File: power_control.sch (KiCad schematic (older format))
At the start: 80 parts, among them J1 Conn_01x02, J2 Conn_01x02, J28 Conn_01x02, J29 Conn_01x02, J30 Conn_01x02, J4 Conn_01x02, J5 Conn_01x02, J6 Conn_01x02, U1 L6203, U10 L6203, U11 L6203, U12 L6203, U3 L6203, U5 L6203, U6 L6203, U7 L6203

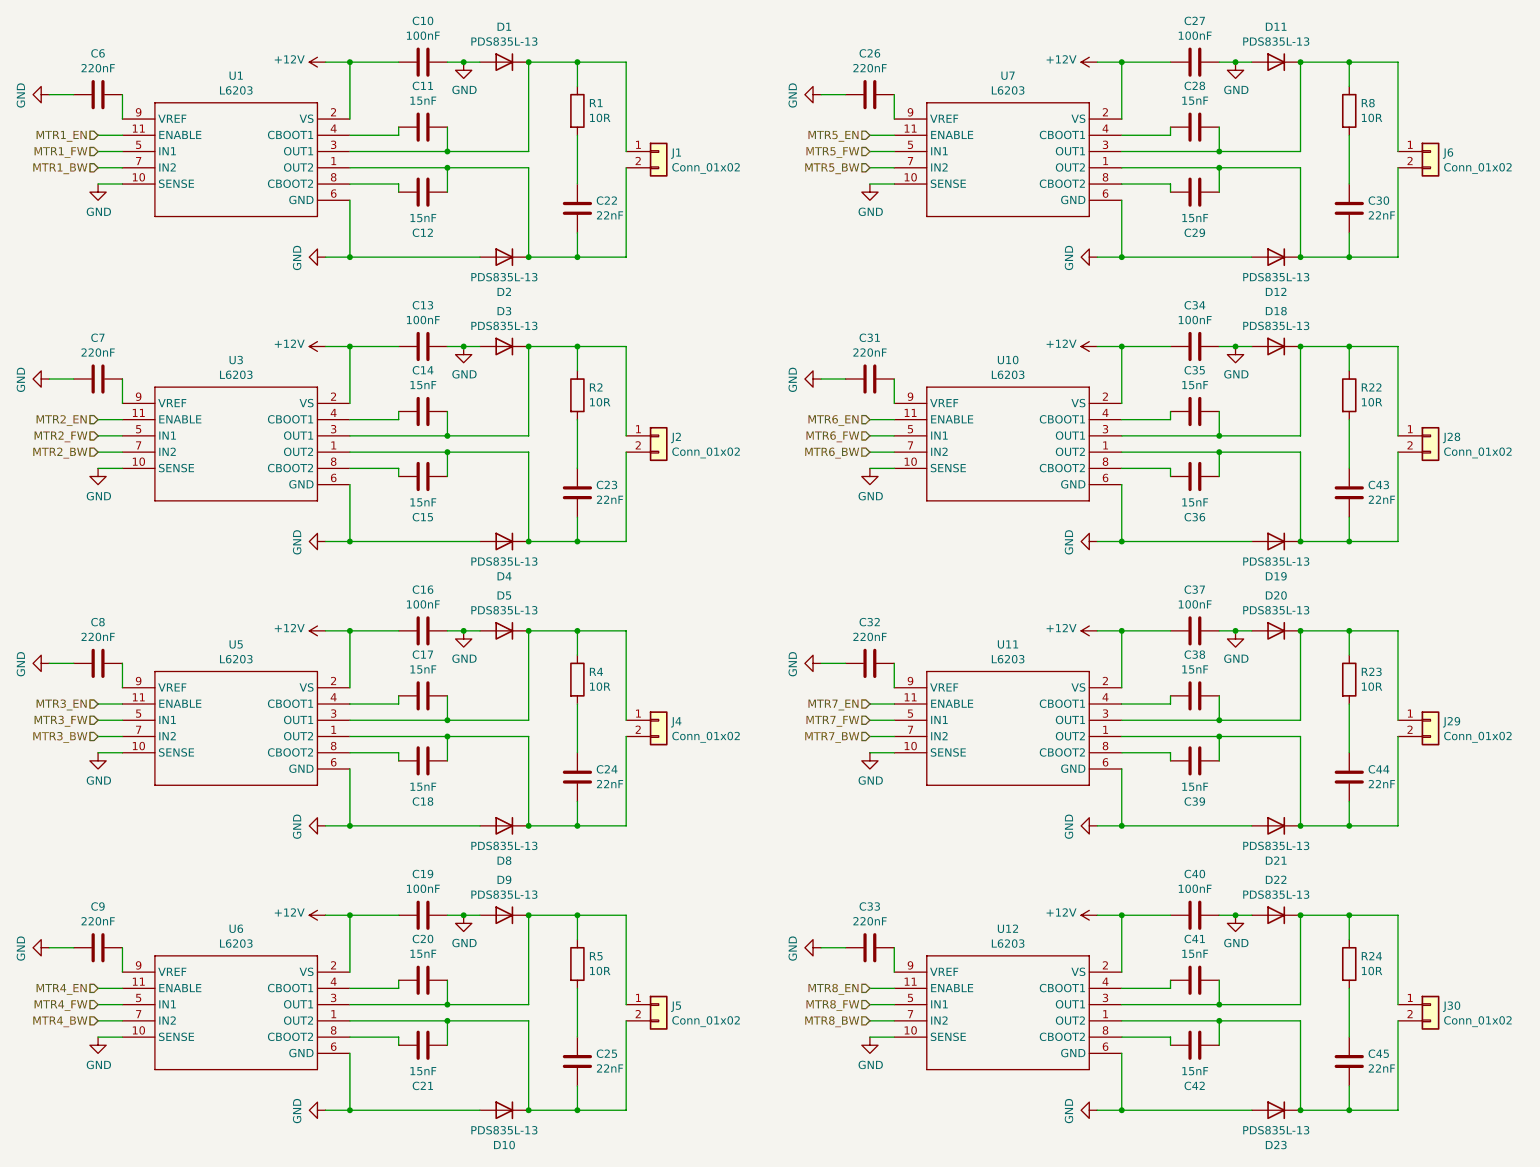
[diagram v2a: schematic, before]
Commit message: Positioning finished
Lacks fine alignment.
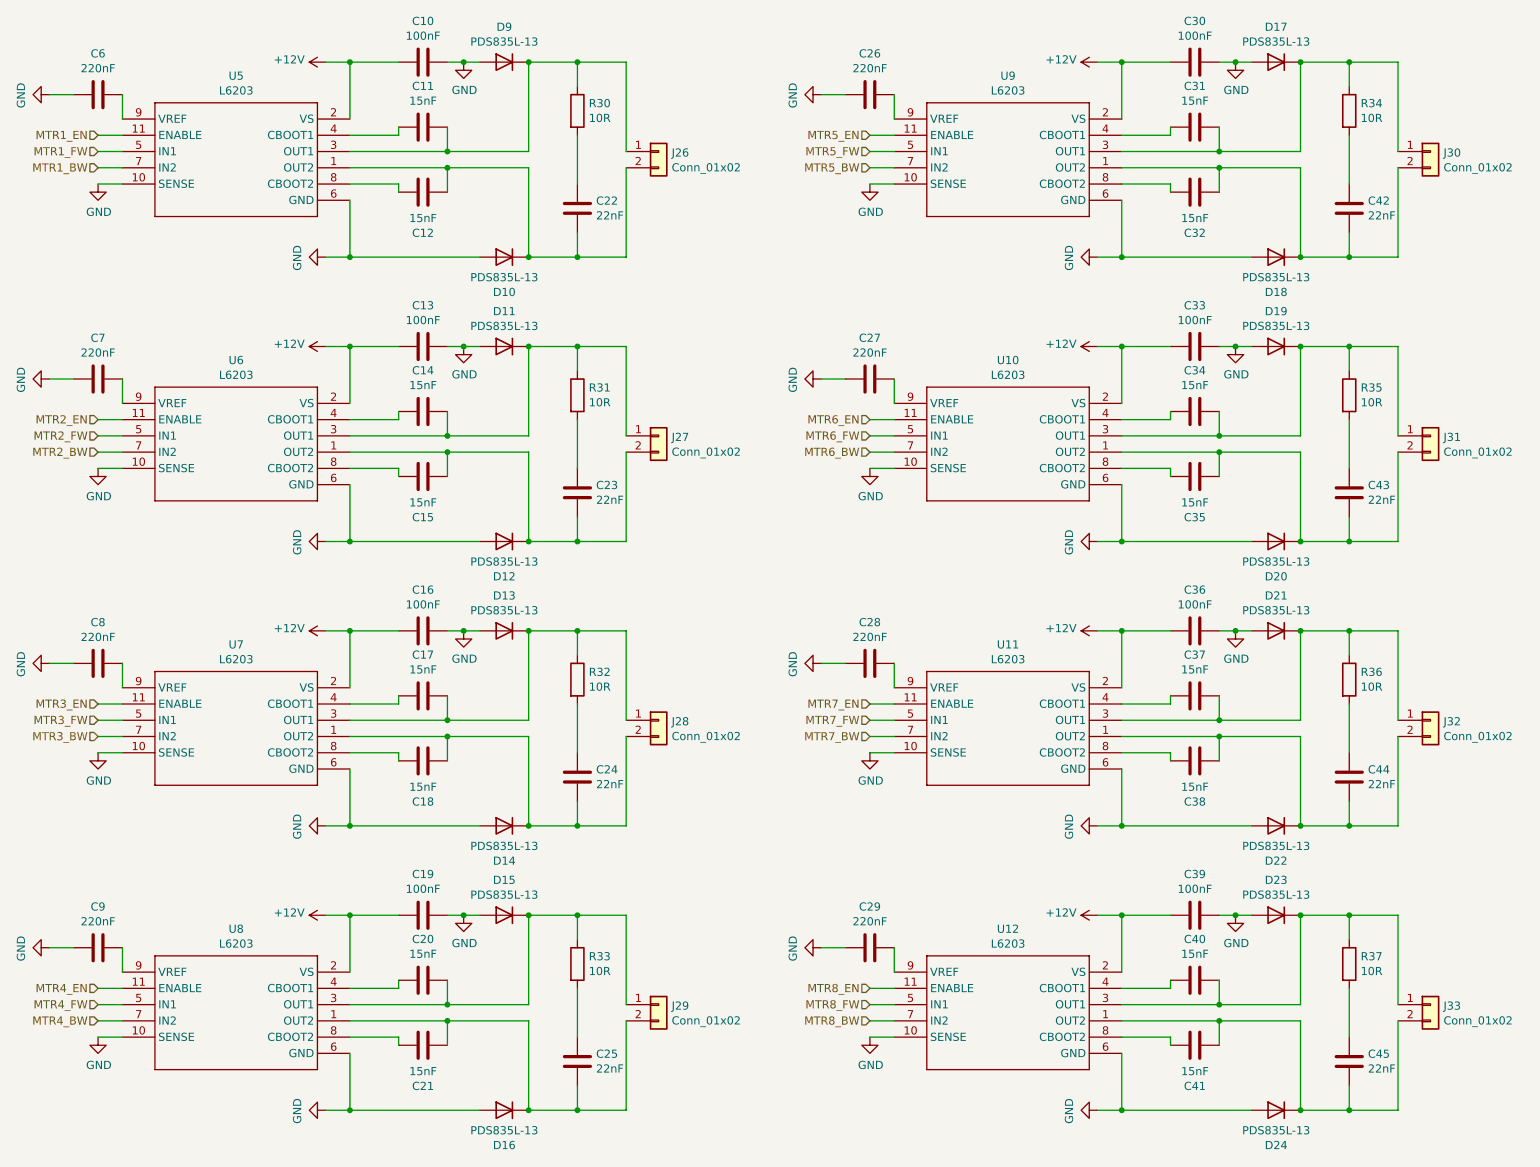
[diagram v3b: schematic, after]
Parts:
- renumbered C31 to C27, C32 to C28, C33 to C29, C27 to C30, C28 to C31, C29 to C32, C34 to C33, C35 to C34, C36 to C35, C37 to C36, C38 to C37, C39 to C38, C40 to C39, C41 to C40, C42 to C41, C30 to C42, D2 to D10, D3 to D11, D4 to D12, D5 to D13, D8 to D14, D9 to D15, D10 to D16, D11 to D17, D12 to D18, D18 to D19, D19 to D20, D20 to D21, D21 to D22, D22 to D23, D23 to D24, D1 to D9, J1 to J26, J2 to J27, J4 to J28, J5 to J29, J6 to J30, J28 to J31, J29 to J32, J30 to J33, R1 to R30, R2 to R31, R4 to R32, R5 to R33, R8 to R34, R22 to R35, R23 to R36, R24 to R37, U1 to U5, U3 to U6, U5 to U7, U6 to U8, U7 to U9

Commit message: Start MCU layout
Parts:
- renumbered C6 to C11, C7 to C12, C8 to C13, C9 to C14, C10 to C15, C11 to C16, C12 to C17, C13 to C18, C14 to C19, C15 to C20, C16 to C21, C17 to C22, C18 to C23, C19 to C24, C20 to C25, C21 to C26, C22 to C27, C23 to C28, C24 to C29, C25 to C30, C26 to C31, C27 to C32, C28 to C33, C29 to C34, C30 to C35, C31 to C36, C32 to C37, C33 to C38, C34 to C39, C35 to C40, C36 to C41, C37 to C42, C38 to C43, C39 to C44, C40 to C45, C41 to C46, C42 to C47, C43 to C48, C44 to C49, C45 to C50, J26 to J27, J27 to J28, J28 to J29, J29 to J30, J30 to J31, J31 to J32, J32 to J33, J33 to J34

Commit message: Stash
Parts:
- renumbered J27 to J26, J28 to J27, J29 to J28, J30 to J29, J31 to J30, J32 to J31, J33 to J32, J34 to J33
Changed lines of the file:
@@
 P 4450 6550
 AR Path="/5E1FFE0F" Ref="J?"  Part="1"
-AR Path="/5E1C04CF/5E1FFE0F" Ref="J30"  Part="1"
+AR Path="/5E1C04CF/5E1FFE0F" Ref="J29"  Part="1"
 AR Path="/5E3E0C4B/5E1FFE0F" Ref="J?"  Part="1"
-F 0 "J30" H 4530 6542 50  0000 L CNN
+F 0 "J29" H 4530 6542 50  0000 L CNN
 F 1 "Conn_01x02" H 4530 6451 50  0000 L CNN
 F 2 "Connector_Molex:Molex_Micro-Fit_3.0_43045-0212_2x01_P3.00mm_Vertical" H 4450 6550 50  0001 C CNN
@@
 P 4450 4800
 AR Path="/5E4C5662" Ref="J?"  Part="1"
-AR Path="/5E1C04CF/5E4C5662" Ref="J29"  Part="1"
+AR Path="/5E1C04CF/5E4C5662" Ref="J28"  Part="1"
 AR Path="/5E3E0C4B/5E4C5662" Ref="J?"  Part="1"
-F 0 "J29" H 4530 4792 50  0000 L CNN
+F 0 "J28" H 4530 4792 50  0000 L CNN
 F 1 "Conn_01x02" H 4530 4701 50  0000 L CNN
 F 2 "Connector_Molex:Molex_Micro-Fit_3.0_43045-0212_2x01_P3.00mm_Vertical" H 4450 4800 50  0001 C CNN
@@
 P 4450 3050
 AR Path="/5E4D6D0D" Ref="J?"  Part="1"
-AR Path="/5E1C04CF/5E4D6D0D" Ref="J28"  Part="1"
+AR Path="/5E1C04CF/5E4D6D0D" Ref="J27"  Part="1"
 AR Path="/5E3E0C4B/5E4D6D0D" Ref="J?"  Part="1"
-F 0 "J28" H 4530 3042 50  0000 L CNN
+F 0 "J27" H 4530 3042 50  0000 L CNN
 F 1 "Conn_01x02" H 4530 2951 50  0000 L CNN
 F 2 "Connector_Molex:Molex_Micro-Fit_3.0_43045-0212_2x01_P3.00mm_Vertical" H 4450 3050 50  0001 C CNN
@@
 P 9200 1300
 AR Path="/5E50C463" Ref="J?"  Part="1"
-AR Path="/5E1C04CF/5E50C463" Ref="J31"  Part="1"
+AR Path="/5E1C04CF/5E50C463" Ref="J30"  Part="1"
 AR Path="/5E3E0C4B/5E50C463" Ref="J?"  Part="1"
-F 0 "J31" H 9280 1292 50  0000 L CNN
+F 0 "J30" H 9280 1292 50  0000 L CNN
 F 1 "Conn_01x02" H 9280 1201 50  0000 L CNN
 F 2 "Connector_Molex:Molex_Micro-Fit_3.0_43045-0212_2x01_P3.00mm_Vertical" H 9200 1300 50  0001 C CNN
@@
 P 9200 6550
 AR Path="/5E42316A" Ref="J?"  Part="1"
-AR Path="/5E1C04CF/5E42316A" Ref="J34"  Part="1"
+AR Path="/5E1C04CF/5E42316A" Ref="J33"  Part="1"
 AR Path="/5E3E0C4B/5E42316A" Ref="J?"  Part="1"
-F 0 "J34" H 9280 6542 50  0000 L CNN
+F 0 "J33" H 9280 6542 50  0000 L CNN
 F 1 "Conn_01x02" H 9280 6451 50  0000 L CNN
 F 2 "Connector_Molex:Molex_Micro-Fit_3.0_43045-0212_2x01_P3.00mm_Vertical" H 9200 6550 50  0001 C CNN
@@
 P 9200 4800
 AR Path="/5E4231F1" Ref="J?"  Part="1"
-AR Path="/5E1C04CF/5E4231F1" Ref="J33"  Part="1"
+AR Path="/5E1C04CF/5E4231F1" Ref="J32"  Part="1"
 AR Path="/5E3E0C4B/5E4231F1" Ref="J?"  Part="1"
-F 0 "J33" H 9280 4792 50  0000 L CNN
+F 0 "J32" H 9280 4792 50  0000 L CNN
 F 1 "Conn_01x02" H 9280 4701 50  0000 L CNN
 F 2 "Connector_Molex:Molex_Micro-Fit_3.0_43045-0212_2x01_P3.00mm_Vertical" H 9200 4800 50  0001 C CNN
@@
 P 9200 3050
 AR Path="/5E42327E" Ref="J?"  Part="1"
-AR Path="/5E1C04CF/5E42327E" Ref="J32"  Part="1"
+AR Path="/5E1C04CF/5E42327E" Ref="J31"  Part="1"
 AR Path="/5E3E0C4B/5E42327E" Ref="J?"  Part="1"
-F 0 "J32" H 9280 3042 50  0000 L CNN
+F 0 "J31" H 9280 3042 50  0000 L CNN
 F 1 "Conn_01x02" H 9280 2951 50  0000 L CNN
 F 2 "Connector_Molex:Molex_Micro-Fit_3.0_43045-0212_2x01_P3.00mm_Vertical" H 9200 3050 50  0001 C CNN
@@
 P 4450 1300
 AR Path="/5E4D6D98" Ref="J?"  Part="1"
-AR Path="/5E1C04CF/5E4D6D98" Ref="J27"  Part="1"
+AR Path="/5E1C04CF/5E4D6D98" Ref="J26"  Part="1"
 AR Path="/5E3E0C4B/5E4D6D98" Ref="J?"  Part="1"
-F 0 "J27" H 4530 1292 50  0000 L CNN
+F 0 "J26" H 4530 1292 50  0000 L CNN
 F 1 "Conn_01x02" H 4530 1201 50  0000 L CNN
 F 2 "Connector_Molex:Molex_Micro-Fit_3.0_43045-0212_2x01_P3.00mm_Vertical" H 4450 1300 50  0001 C CNN

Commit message: Added capacitor references
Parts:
- C11, C12, C13, C14, C31, C32, C33, C34: manf# (none) -> EMK107B7224KA-T
- C15, C18, C21, C24, C35, C38, C41, C44: manf# (none) -> EMK107B7104KAHT
- C16, C17, C19, C20, C22, C23, C25, C26, C36, C37, C39, C40, C42, C43, C45, C46: manf# (none) -> C0603C153M4RECTU
- C27, C28, C29, C30, C47, C48, C49, C50: manf# (none) -> C0603C223K4RACTU
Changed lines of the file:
@@
 F 2 "lsts-passives:C_0603" H 1038 6050 50  0001 C CNN
 F 3 "~" H 1000 6200 50  0001 C CNN
+F 4 "EMK107B7224KA-T" H 1000 6200 50  0001 C CNN "manf#"
 	1    1000 6200
 	0    1    1    0
@@
 F 2 "lsts-passives:C_0603" H 3988 6750 50  0001 C CNN
 F 3 "~" H 3950 6900 50  0001 C CNN
+F 4 "C0603C223K4RACTU" H 3950 6900 50  0001 C CNN "manf#"
 	1    3950 6900
 	1    0    0    -1
@@
 F 2 "lsts-passives:C_0603" H 3038 6250 50  0001 C CNN
 F 3 "~" H 3000 6400 50  0001 C CNN
+F 4 "C0603C153M4RECTU" H 3000 6400 50  0001 C CNN "manf#"
 	1    3000 6400
 	0    1    1    0
@@
 F 2 "lsts-passives:C_0603" H 3038 6650 50  0001 C CNN
 F 3 "~" H 3000 6800 50  0001 C CNN
+F 4 "C0603C153M4RECTU" H 3000 6800 50  0001 C CNN "manf#"
 	1    3000 6800
 	0    1    -1   0
@@
 F 2 "lsts-passives:C_0603" H 3038 5850 50  0001 C CNN
 F 3 "~" H 3000 6000 50  0001 C CNN
+F 4 "EMK107B7104KAHT" H 3000 6000 50  0001 C CNN "manf#"
 	1    3000 6000
 	0    1    1    0
@@
 F 2 "lsts-passives:C_0603" H 1038 4300 50  0001 C CNN
 F 3 "~" H 1000 4450 50  0001 C CNN
+F 4 "EMK107B7224KA-T" H 1000 4450 50  0001 C CNN "manf#"
 	1    1000 4450
 	0    1    1    0
@@
 F 2 "lsts-passives:C_0603" H 3038 4500 50  0001 C CNN
 F 3 "~" H 3000 4650 50  0001 C CNN
+F 4 "C0603C153M4RECTU" H 3000 4650 50  0001 C CNN "manf#"
 	1    3000 4650
 	0    1    1    0
@@
 F 2 "lsts-passives:C_0603" H 3038 4900 50  0001 C CNN
 F 3 "~" H 3000 5050 50  0001 C CNN
+F 4 "C0603C153M4RECTU" H 3000 5050 50  0001 C CNN "manf#"
 	1    3000 5050
 	0    1    -1   0
@@
 F 2 "lsts-passives:C_0603" H 3038 4100 50  0001 C CNN
 F 3 "~" H 3000 4250 50  0001 C CNN
+F 4 "EMK107B7104KAHT" H 3000 4250 50  0001 C CNN "manf#"
 	1    3000 4250
 	0    1    1    0
@@
 F 2 "lsts-passives:C_0603" H 1038 2550 50  0001 C CNN
 F 3 "~" H 1000 2700 50  0001 C CNN
+F 4 "EMK107B7224KA-T" H 1000 2700 50  0001 C CNN "manf#"
 	1    1000 2700
 	0    1    1    0
@@
 F 2 "lsts-passives:C_0603" H 3988 3250 50  0001 C CNN
 F 3 "~" H 3950 3400 50  0001 C CNN
+F 4 "C0603C223K4RACTU" H 3950 3400 50  0001 C CNN "manf#"
 	1    3950 3400
 	1    0    0    -1
@@
 F 2 "lsts-passives:C_0603" H 3038 2750 50  0001 C CNN
 F 3 "~" H 3000 2900 50  0001 C CNN
+F 4 "C0603C153M4RECTU" H 3000 2900 50  0001 C CNN "manf#"
 	1    3000 2900
 	0    1    1    0
@@
 F 2 "lsts-passives:C_0603" H 3038 3150 50  0001 C CNN
 F 3 "~" H 3000 3300 50  0001 C CNN
+F 4 "C0603C153M4RECTU" H 3000 3300 50  0001 C CNN "manf#"
 	1    3000 3300
 	0    1    -1   0
@@
 F 2 "lsts-passives:C_0603" H 3038 2350 50  0001 C CNN
 F 3 "~" H 3000 2500 50  0001 C CNN
+F 4 "EMK107B7104KAHT" H 3000 2500 50  0001 C CNN "manf#"
 	1    3000 2500
 	0    1    1    0
@@
 F 2 "lsts-passives:C_0603" H 5788 800 50  0001 C CNN
 F 3 "~" H 5750 950 50  0001 C CNN
+F 4 "EMK107B7224KA-T" H 5750 950 50  0001 C CNN "manf#"
 	1    5750 950
 	0    1    1    0
@@
 F 2 "lsts-passives:C_0603" H 8738 1500 50  0001 C CNN
 F 3 "~" H 8700 1650 50  0001 C CNN
+F 4 "C0603C223K4RACTU" H 8700 1650 50  0001 C CNN "manf#"
 	1    8700 1650
 	1    0    0    -1
@@
 F 2 "lsts-passives:C_0603" H 7788 1000 50  0001 C CNN
 F 3 "~" H 7750 1150 50  0001 C CNN
+F 4 "C0603C153M4RECTU" H 7750 1150 50  0001 C CNN "manf#"
 	1    7750 1150
 	0    1    1    0
@@
 F 2 "lsts-passives:C_0603" H 7788 1400 50  0001 C CNN
 F 3 "~" H 7750 1550 50  0001 C CNN
+F 4 "C0603C153M4RECTU" H 7750 1550 50  0001 C CNN "manf#"
 	1    7750 1550
 	0    1    -1   0
@@
 F 2 "lsts-passives:C_0603" H 7788 600 50  0001 C CNN
 F 3 "~" H 7750 750 50  0001 C CNN
+F 4 "EMK107B7104KAHT" H 7750 750 50  0001 C CNN "manf#"
 	1    7750 750
 	0    1    1    0
@@
 F 2 "lsts-passives:C_0603" H 3988 5000 50  0001 C CNN
 F 3 "~" H 3950 5150 50  0001 C CNN
+F 4 "C0603C223K4RACTU" H 3950 5150 50  0001 C CNN "manf#"
 	1    3950 5150
 	1    0    0    -1
@@
 F 2 "lsts-passives:C_0603" H 5788 6050 50  0001 C CNN
 F 3 "~" H 5750 6200 50  0001 C CNN
+F 4 "EMK107B7224KA-T" H 5750 6200 50  0001 C CNN "manf#"
 	1    5750 6200
 	0    1    1    0
@@
 F 2 "lsts-passives:C_0603" H 8738 6750 50  0001 C CNN
 F 3 "~" H 8700 6900 50  0001 C CNN
+F 4 "C0603C223K4RACTU" H 8700 6900 50  0001 C CNN "manf#"
 	1    8700 6900
 	1    0    0    -1
@@
 F 2 "lsts-passives:C_0603" H 7788 6250 50  0001 C CNN
 F 3 "~" H 7750 6400 50  0001 C CNN
+F 4 "C0603C153M4RECTU" H 7750 6400 50  0001 C CNN "manf#"
 	1    7750 6400
 	0    1    1    0
@@
 F 2 "lsts-passives:C_0603" H 7788 6650 50  0001 C CNN
 F 3 "~" H 7750 6800 50  0001 C CNN
+F 4 "C0603C153M4RECTU" H 7750 6800 50  0001 C CNN "manf#"
 	1    7750 6800
 	0    1    -1   0
@@
 F 2 "lsts-passives:C_0603" H 7788 5850 50  0001 C CNN
 F 3 "~" H 7750 6000 50  0001 C CNN
+F 4 "EMK107B7104KAHT" H 7750 6000 50  0001 C CNN "manf#"
 	1    7750 6000
 	0    1    1    0
@@
 F 2 "lsts-passives:C_0603" H 5788 4300 50  0001 C CNN
 F 3 "~" H 5750 4450 50  0001 C CNN
+F 4 "EMK107B7224KA-T" H 5750 4450 50  0001 C CNN "manf#"
 	1    5750 4450
 	0    1    1    0
@@
 F 2 "lsts-passives:C_0603" H 7788 4500 50  0001 C CNN
 F 3 "~" H 7750 4650 50  0001 C CNN
+F 4 "C0603C153M4RECTU" H 7750 4650 50  0001 C CNN "manf#"
 	1    7750 4650
 	0    1    1    0
@@
 F 2 "lsts-passives:C_0603" H 7788 4900 50  0001 C CNN
 F 3 "~" H 7750 5050 50  0001 C CNN
+F 4 "C0603C153M4RECTU" H 7750 5050 50  0001 C CNN "manf#"
 	1    7750 5050
 	0    1    -1   0
@@
 F 2 "lsts-passives:C_0603" H 7788 4100 50  0001 C CNN
 F 3 "~" H 7750 4250 50  0001 C CNN
+F 4 "EMK107B7104KAHT" H 7750 4250 50  0001 C CNN "manf#"
 	1    7750 4250
 	0    1    1    0
@@
 F 2 "lsts-passives:C_0603" H 5788 2550 50  0001 C CNN
 F 3 "~" H 5750 2700 50  0001 C CNN
+F 4 "EMK107B7224KA-T" H 5750 2700 50  0001 C CNN "manf#"
 	1    5750 2700
 	0    1    1    0
@@
 F 2 "lsts-passives:C_0603" H 8738 3250 50  0001 C CNN
 F 3 "~" H 8700 3400 50  0001 C CNN
+F 4 "C0603C223K4RACTU" H 8700 3400 50  0001 C CNN "manf#"
 	1    8700 3400
 	1    0    0    -1
@@
 F 2 "lsts-passives:C_0603" H 7788 2750 50  0001 C CNN
 F 3 "~" H 7750 2900 50  0001 C CNN
+F 4 "C0603C153M4RECTU" H 7750 2900 50  0001 C CNN "manf#"
 	1    7750 2900
 	0    1    1    0
@@
 F 2 "lsts-passives:C_0603" H 7788 3150 50  0001 C CNN
 F 3 "~" H 7750 3300 50  0001 C CNN
+F 4 "C0603C153M4RECTU" H 7750 3300 50  0001 C CNN "manf#"
 	1    7750 3300
 	0    1    -1   0
@@
 F 2 "lsts-passives:C_0603" H 7788 2350 50  0001 C CNN
 F 3 "~" H 7750 2500 50  0001 C CNN
+F 4 "EMK107B7104KAHT" H 7750 2500 50  0001 C CNN "manf#"
 	1    7750 2500
 	0    1    1    0
@@
 F 2 "lsts-passives:C_0603" H 8738 5000 50  0001 C CNN
 F 3 "~" H 8700 5150 50  0001 C CNN
+F 4 "C0603C223K4RACTU" H 8700 5150 50  0001 C CNN "manf#"
 	1    8700 5150
 	1    0    0    -1
@@
 F 2 "lsts-passives:C_0603" H 3038 600 50  0001 C CNN
 F 3 "~" H 3000 750 50  0001 C CNN
+F 4 "EMK107B7104KAHT" H 3000 750 50  0001 C CNN "manf#"
 	1    3000 750
 	0    1    1    0
@@
 F 2 "lsts-passives:C_0603" H 3038 1400 50  0001 C CNN
 F 3 "~" H 3000 1550 50  0001 C CNN
+F 4 "C0603C153M4RECTU" H 3000 1550 50  0001 C CNN "manf#"
 	1    3000 1550
 	0    1    -1   0
@@
 F 2 "lsts-passives:C_0603" H 3038 1000 50  0001 C CNN
 F 3 "~" H 3000 1150 50  0001 C CNN
+F 4 "C0603C153M4RECTU" H 3000 1150 50  0001 C CNN "manf#"
 	1    3000 1150
 	0    1    1    0
@@
 F 2 "lsts-passives:C_0603" H 3988 1500 50  0001 C CNN
 F 3 "~" H 3950 1650 50  0001 C CNN
+F 4 "C0603C223K4RACTU" H 3950 1650 50  0001 C CNN "manf#"
 	1    3950 1650
 	1    0    0    -1
@@
 F 2 "lsts-passives:C_0603" H 1038 800 50  0001 C CNN
 F 3 "~" H 1000 950 50  0001 C CNN
+F 4 "EMK107B7224KA-T" H 1000 950 50  0001 C CNN "manf#"
 	1    1000 950
 	0    1    1    0

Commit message: Added remaining 0603 references
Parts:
- R30, R31, R32, R33, R34, R35, R36, R37: manf# (none) -> CRCW060310R0FKEAC
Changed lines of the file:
@@
 F 2 "lsts-passives:R_0603" V 3880 6300 50  0001 C CNN
 F 3 "~" H 3950 6300 50  0001 C CNN
+F 4 "CRCW060310R0FKEAC" H 3950 6300 50  0001 C CNN "manf#"
 	1    3950 6300
 	1    0    0    -1
@@
 F 2 "lsts-passives:R_0603" V 3880 4550 50  0001 C CNN
 F 3 "~" H 3950 4550 50  0001 C CNN
+F 4 "CRCW060310R0FKEAC" H 3950 4550 50  0001 C CNN "manf#"
 	1    3950 4550
 	1    0    0    -1
@@
 F 2 "lsts-passives:R_0603" V 3880 2800 50  0001 C CNN
 F 3 "~" H 3950 2800 50  0001 C CNN
+F 4 "CRCW060310R0FKEAC" H 3950 2800 50  0001 C CNN "manf#"
 	1    3950 2800
 	1    0    0    -1
@@
 F 2 "lsts-passives:R_0603" V 8630 1050 50  0001 C CNN
 F 3 "~" H 8700 1050 50  0001 C CNN
+F 4 "CRCW060310R0FKEAC" H 8700 1050 50  0001 C CNN "manf#"
 	1    8700 1050
 	1    0    0    -1
@@
 F 2 "lsts-passives:R_0603" V 8630 6300 50  0001 C CNN
 F 3 "~" H 8700 6300 50  0001 C CNN
+F 4 "CRCW060310R0FKEAC" H 8700 6300 50  0001 C CNN "manf#"
 	1    8700 6300
 	1    0    0    -1
@@
 F 2 "lsts-passives:R_0603" V 8630 4550 50  0001 C CNN
 F 3 "~" H 8700 4550 50  0001 C CNN
+F 4 "CRCW060310R0FKEAC" H 8700 4550 50  0001 C CNN "manf#"
 	1    8700 4550
 	1    0    0    -1
@@
 F 2 "lsts-passives:R_0603" V 8630 2800 50  0001 C CNN
 F 3 "~" H 8700 2800 50  0001 C CNN
+F 4 "CRCW060310R0FKEAC" H 8700 2800 50  0001 C CNN "manf#"
 	1    8700 2800
 	1    0    0    -1
@@
 F 2 "lsts-passives:R_0603" V 3880 1050 50  0001 C CNN
 F 3 "~" H 3950 1050 50  0001 C CNN
+F 4 "CRCW060310R0FKEAC" H 3950 1050 50  0001 C CNN "manf#"
 	1    3950 1050
 	1    0    0    -1
